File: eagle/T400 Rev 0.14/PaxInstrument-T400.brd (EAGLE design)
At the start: 99.1 x 53.3 mm, 137 parts, among them IC1 MCP3424, IC3 SN74LVC1G74DCT, J1 MICRO-SDCARD-CONNECTOR-330006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, Q1 DMP2035U-7, Q2 DMP2035U-7, Q3 DMN2075U-7, Q4 DMN2075U-7, Q5 DMP2035U-7, U1 MCP9800, U2 APX809, U3 MCP73831, U4 MIC5219-3.3V, X1 FH12-12S-1S, Y1 RESONATORSMD

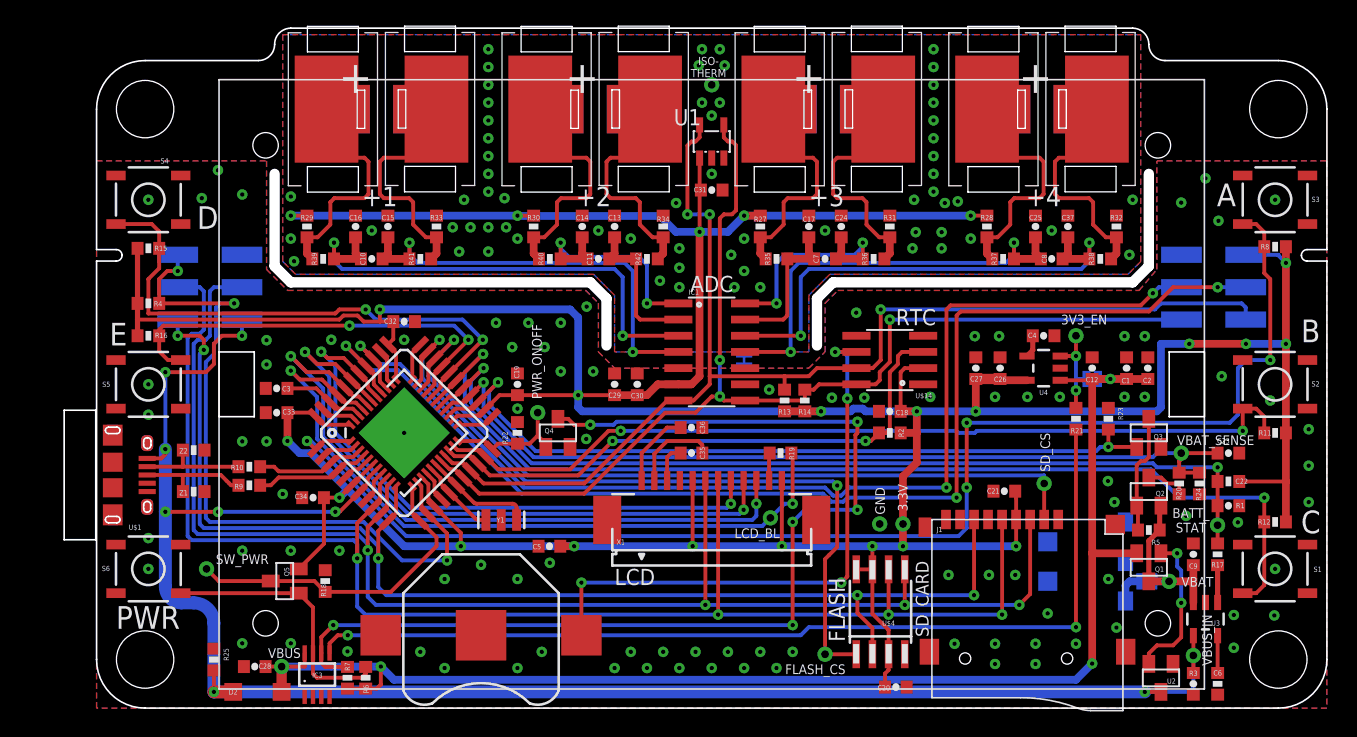
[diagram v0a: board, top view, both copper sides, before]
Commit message: Added T400 location PDF. Moved component names on PCB file.
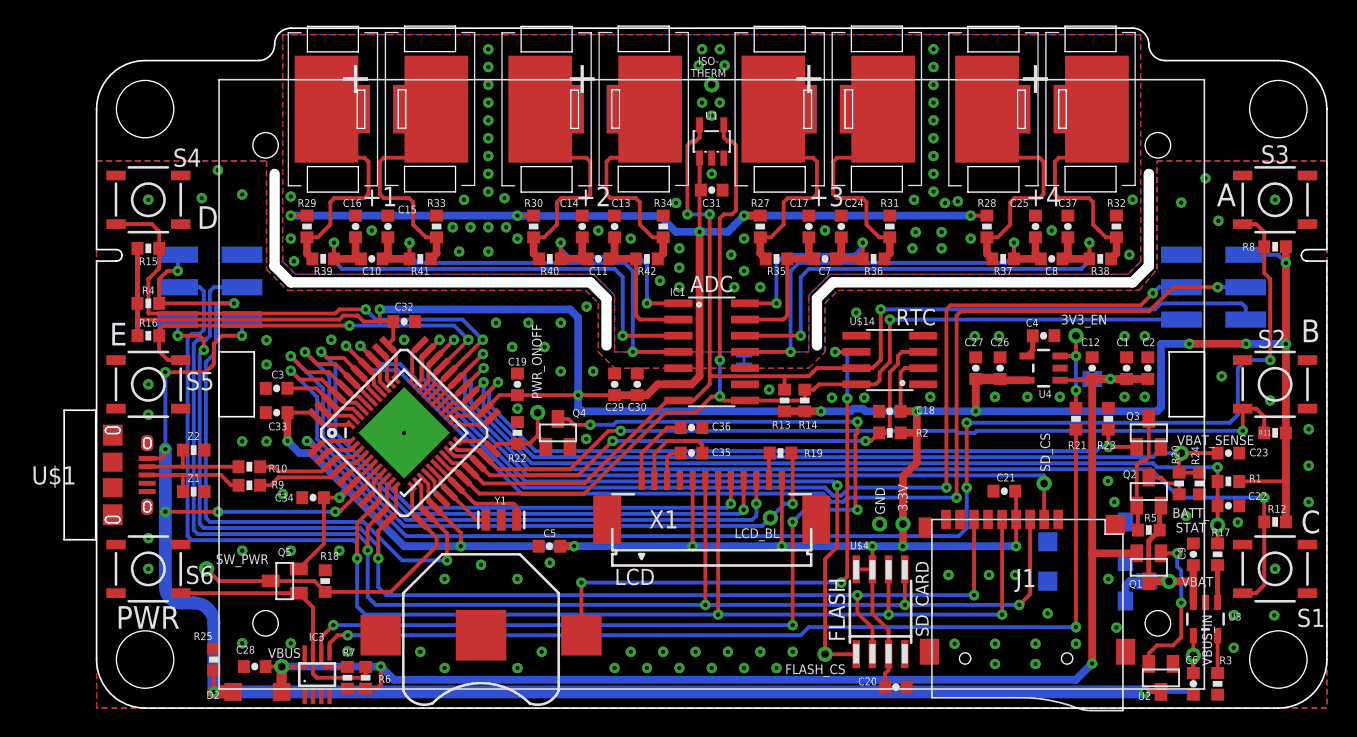
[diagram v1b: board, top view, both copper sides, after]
